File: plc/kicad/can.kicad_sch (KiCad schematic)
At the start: 12 parts, among them CN11 DB2ERC-5.08-4P, J3 Conn_01x02_Pin, SW4 MSK12C02, U18 TCAN337DR

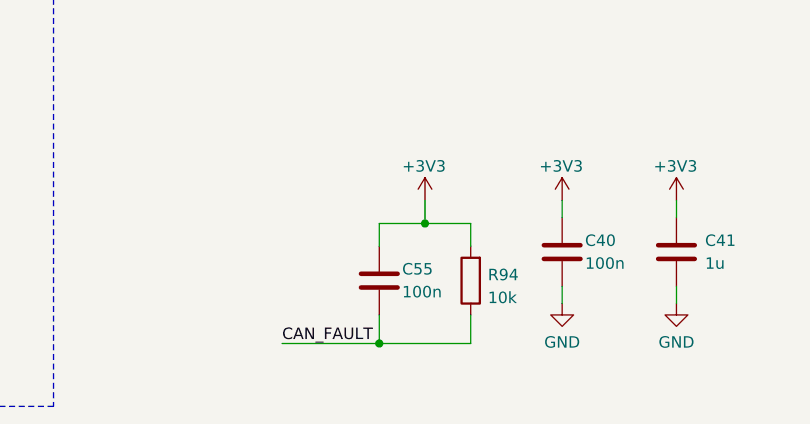
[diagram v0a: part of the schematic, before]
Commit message: Removed CAN FLT resistor
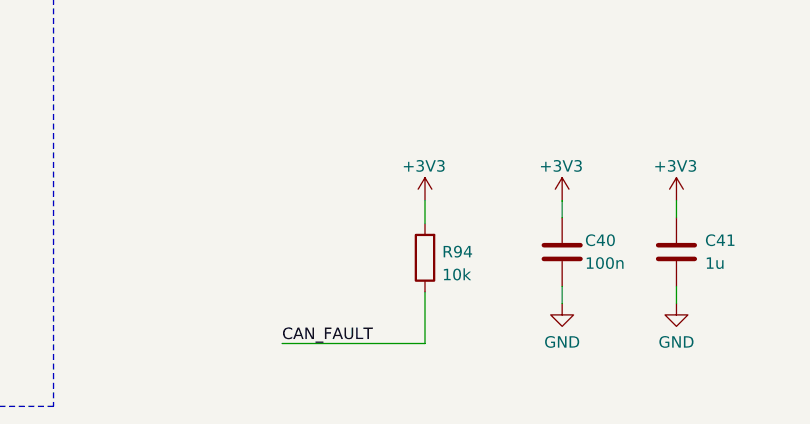
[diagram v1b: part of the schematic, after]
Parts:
- removed C55: 100n, Capacitor_SMD:C_0603_1608Metric, symbol Device:C
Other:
- moved on the sheet: R94
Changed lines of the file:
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@@
-	)
-	(junction
-		(at 160.02 159.385)
-		(diameter 0)
-		(color 0 0 0 0)
-	)
-	(junction
-		(at 165.1 146.05)
-		(diameter 0)
-		(color 0 0 0 0)
 	)
 	(junction
@@
 	(wire
 		(pts
-			(xy 170.18 146.05) (xy 170.18 148.59)
-		)
-		(stroke
-			(width 0)
-			(type default)
-		)
-	)
-	(wire
-		(pts
 			(xy 191.135 89.535) (xy 198.755 89.535)
 		)
@@
 	(wire
 		(pts
-			(xy 160.02 146.05) (xy 165.1 146.05)
-		)
-		(stroke
-			(width 0)
-			(type default)
-		)
-	)
-	(wire
-		(pts
 			(xy 57.15 81.915) (xy 74.295 81.915)
 		)
@@
 	(wire
 		(pts
-			(xy 160.02 156.21) (xy 160.02 159.385)
-		)
-		(stroke
-			(width 0)
-			(type default)
-		)
-	)
-	(wire
-		(pts
-			(xy 165.1 146.05) (xy 170.18 146.05)
-		)
-		(stroke
-			(width 0)
-			(type default)
-		)
-	)
-	(wire
-		(pts
 			(xy 69.215 106.045) (xy 69.215 104.775)
 		)
@@
 	(wire
 		(pts
-			(xy 160.02 159.385) (xy 170.18 159.385)
+			(xy 149.225 159.385) (xy 165.1 159.385)
 		)
 		(stroke
@@
 	(wire
 		(pts
-			(xy 149.225 159.385) (xy 160.02 159.385)
-		)
-		(stroke
-			(width 0)
-			(type default)
-		)
-	)
-	(wire
-		(pts
 			(xy 193.04 145.415) (xy 193.04 143.51)
 		)
@@
 	(wire
 		(pts
-			(xy 160.02 148.59) (xy 160.02 146.05)
-		)
-		(stroke
-			(width 0)
-			(type default)
-		)
-	)
-	(wire
-		(pts
 			(xy 76.835 147.955) (xy 79.375 147.955)
 		)
@@
 	(wire
 		(pts
-			(xy 170.18 159.385) (xy 170.18 156.21)
+			(xy 165.1 159.385) (xy 165.1 153.67)
 		)
 		(stroke
@@
 	)
 	(symbol
-		(lib_id "Device:C")
-		(at 160.02 152.4 0)
-		(unit 1)
-		(body_style 1)
-		(exclude_from_sim no)
-		(in_bom yes)
-		(on_board yes)
-		(in_pos_files yes)
-		(dnp no)
-		(property "Reference" "C55"
-			(at 162.56 151.13 0)
-			(show_name no)
-			(do_not_autoplace no)
-			(effects
-				(font
-					(size 1.27 1.27)
-				)
-				(justify left)
-			)
-		)
-		(property "Value" "100n"
-			(at 162.56 153.67 0)
-			(show_name no)
-			(do_not_autoplace no)
-			(effects
-				(font
-					(size 1.27 1.27)
-				)
-				(justify left)
-			)
-		)
-		(property "Footprint" "Capacitor_SMD:C_0603_1608Metric"
-			(at 160.9852 156.21 0)
-			(hide yes)
-			(show_name no)
-			(do_not_autoplace no)
-			(effects
-				(font
-					(size 1.27 1.27)
-				)
-			)
-		)
-		(property "Datasheet" ""
-			(at 160.02 152.4 0)
-			(hide yes)
-			(show_name no)
-			(do_not_autoplace no)
-			(effects
-				(font
-					(size 1.27 1.27)
-				)
-			)
-		)
-		(property "Description" "Unpolarized capacitor"
-			(at 160.02 152.4 0)
-			(hide yes)
-			(show_name no)
-			(do_not_autoplace no)
-			(effects
-				(font
-					(size 1.27 1.27)
-				)
-			)
-		)
-		(pin "2"
-		)
-		(pin "1"
-		)
-		(instances
-			(project "LibrePLC32"
-				(path "/ef4c1a27-85a3-413a-9f93-a41c4f97eee5/1f15b1b2-5031-4e14-8391-148d71dbf666"
-					(reference "C55")
-					(unit 1)
-				)
-			)
-		)
-	)
-	(symbol
 		(lib_id "LibrePLC32:SM24CANA-02HTG")
 		(at 69.215 97.155 180)
@@
 	(symbol
 		(lib_id "Device:R")
-		(at 170.18 152.4 180)
+		(at 165.1 149.86 180)
 		(unit 1)
 		(body_style 1)
@@
 		(dnp no)
 		(property "Reference" "R94"
-			(at 172.085 151.765 0)
+			(at 167.005 149.225 0)
 			(show_name no)
 			(do_not_autoplace no)
@@
 		)
 		(property "Value" "10k"
-			(at 172.085 154.305 0)
+			(at 167.005 151.765 0)
 			(show_name no)
 			(do_not_autoplace no)
@@
 		)
 		(property "Footprint" "Resistor_SMD:R_0603_1608Metric"
-			(at 171.958 152.4 90)
+			(at 166.878 149.86 90)
 			(hide yes)
 			(show_name no)
@@
 		)
 		(property "Datasheet" ""
-			(at 170.18 152.4 0)
+			(at 165.1 149.86 0)
 			(hide yes)
 			(show_name no)
@@
 		)
 		(property "Description" "Resistor"
-			(at 170.18 152.4 0)
-			(hide yes)
-			(show_name no)
+			(at 165.1 149.86 0)
+			(hide yes)
+			(show_name no)

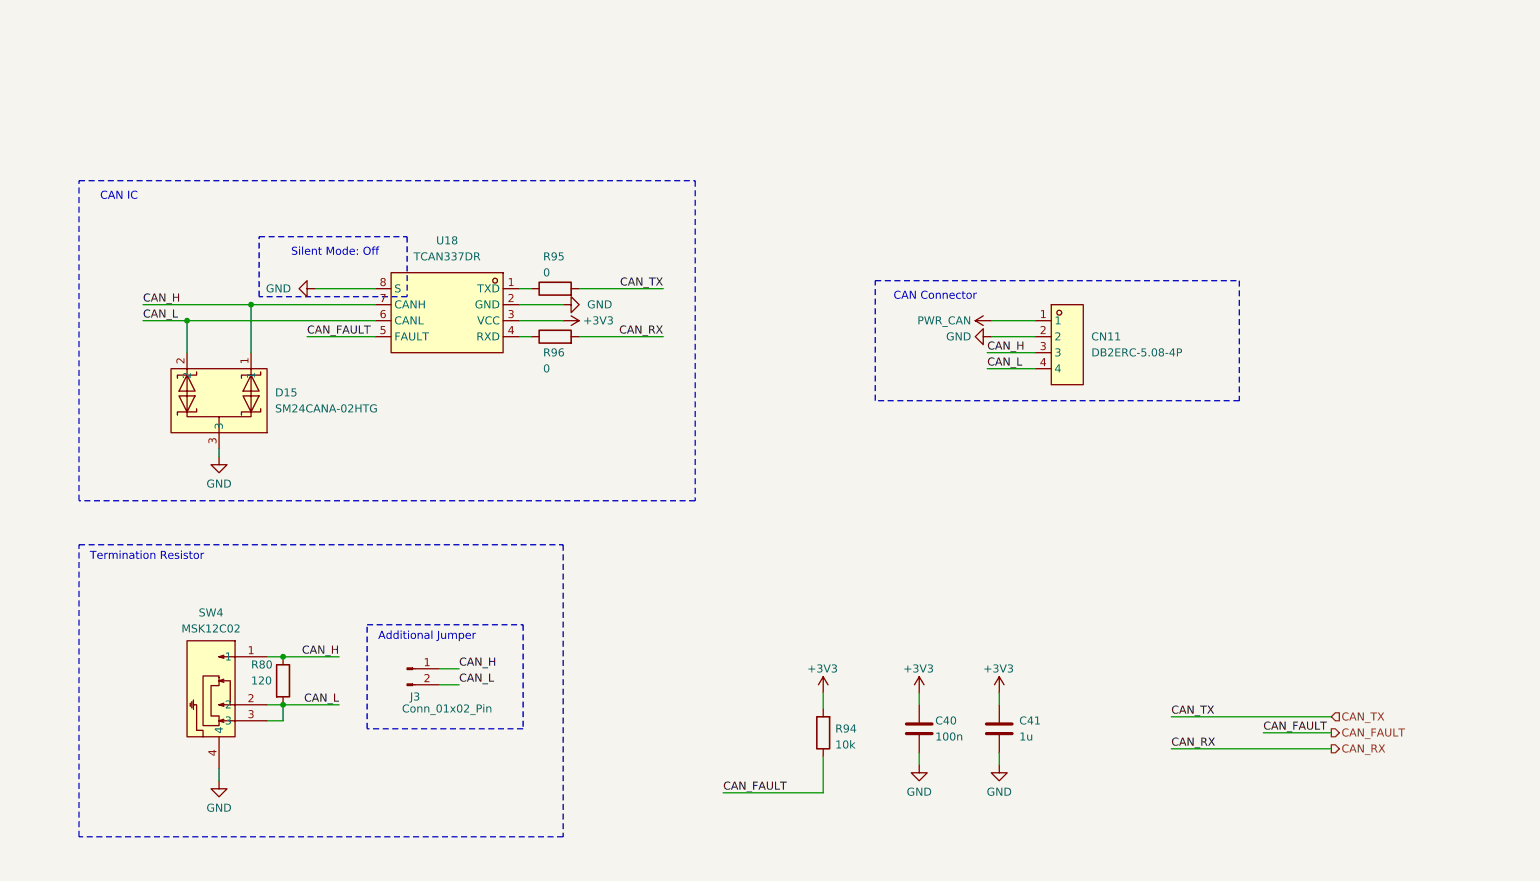
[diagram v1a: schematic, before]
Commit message: Rearranged small PCB placements
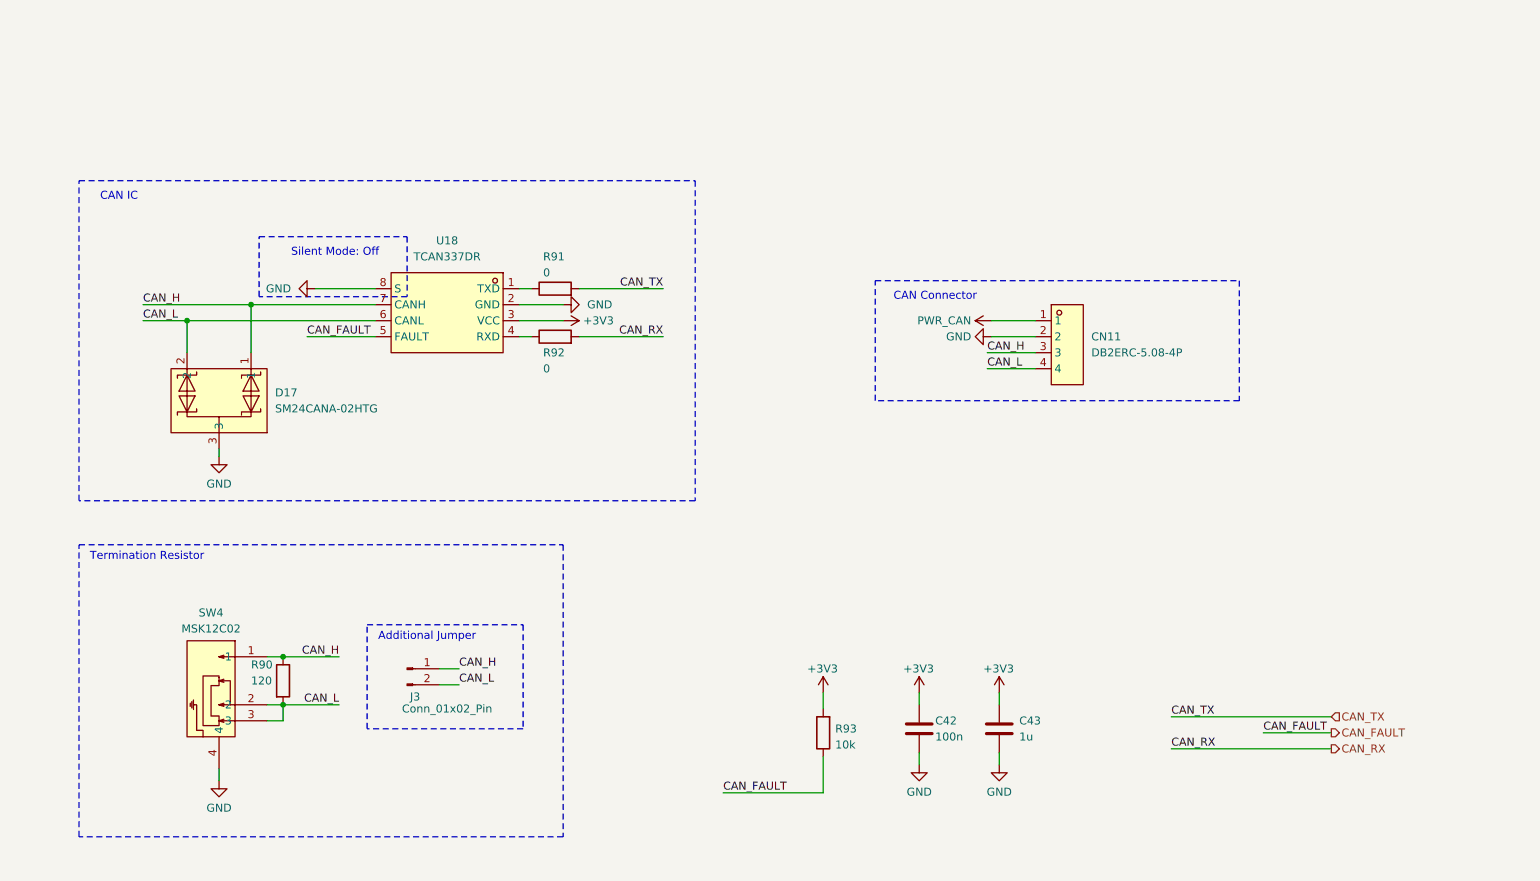
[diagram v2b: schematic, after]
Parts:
- renumbered C40 to C42, C41 to C43, D15 to D17, R80 to R90, R95 to R91, R96 to R92, R94 to R93
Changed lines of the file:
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@@
 		(in_pos_files yes)
 		(dnp no)
-		(property "Reference" "#PWR0199"
+		(property "Reference" "#PWR0212"
 			(at 193.04 147.32 0)
 			(hide yes)
@@
 			(project "LibrePLC32"
 				(path "/ef4c1a27-85a3-413a-9f93-a41c4f97eee5/1f15b1b2-5031-4e14-8391-148d71dbf666"
-					(reference "#PWR0199")
+					(reference "#PWR0212")
 					(unit 1)
 				)
@@
 		(dnp no)
 		(fields_autoplaced yes)
-		(property "Reference" "#PWR0200"
+		(property "Reference" "#PWR0213"
 			(at 193.04 161.29 0)
 			(hide yes)
@@
 			(project "LibrePLC32"
 				(path "/ef4c1a27-85a3-413a-9f93-a41c4f97eee5/1f15b1b2-5031-4e14-8391-148d71dbf666"
-					(reference "#PWR0200")
+					(reference "#PWR0213")
 					(unit 1)
 				)
@@
 		(in_pos_files yes)
 		(dnp no)
-		(property "Reference" "#PWR0192"
+		(property "Reference" "#PWR0204"
 			(at 78.105 79.375 0)
 			(hide yes)
@@
 			(project "LibrePLC32"
 				(path "/ef4c1a27-85a3-413a-9f93-a41c4f97eee5/1f15b1b2-5031-4e14-8391-148d71dbf666"
-					(reference "#PWR0192")
+					(reference "#PWR0204")
 					(unit 1)
 				)
@@
 		(in_pos_files yes)
 		(dnp no)
-		(property "Reference" "#PWR0247"
+		(property "Reference" "#PWR0207"
 			(at 165.1 147.32 0)
 			(hide yes)
@@
 			(project "LibrePLC32"
 				(path "/ef4c1a27-85a3-413a-9f93-a41c4f97eee5/1f15b1b2-5031-4e14-8391-148d71dbf666"
-					(reference "#PWR0247")
+					(reference "#PWR0207")
 					(unit 1)
 				)
@@
 		(dnp no)
 		(fields_autoplaced yes)
-		(property "Reference" "#PWR0190"
+		(property "Reference" "#PWR0203"
 			(at 69.215 163.83 0)
 			(hide yes)
@@
 			(project "LibrePLC32"
 				(path "/ef4c1a27-85a3-413a-9f93-a41c4f97eee5/1f15b1b2-5031-4e14-8391-148d71dbf666"
-					(reference "#PWR0190")
+					(reference "#PWR0203")
 					(unit 1)
 				)
@@
 		(dnp no)
 		(fields_autoplaced yes)
-		(property "Reference" "D15"
+		(property "Reference" "D17"
 			(at 78.105 95.8849 0)
 			(show_name no)
@@
 			(project "LibrePLC32"
 				(path "/ef4c1a27-85a3-413a-9f93-a41c4f97eee5/1f15b1b2-5031-4e14-8391-148d71dbf666"
-					(reference "D15")
+					(reference "D17")
 					(unit 1)
 				)
@@
 		(in_pos_files yes)
 		(dnp no)
-		(property "Reference" "#PWR0194"
+		(property "Reference" "#PWR0206"
 			(at 120.015 84.455 0)
 			(hide yes)
@@
 			(project "LibrePLC32"
 				(path "/ef4c1a27-85a3-413a-9f93-a41c4f97eee5/1f15b1b2-5031-4e14-8391-148d71dbf666"
-					(reference "#PWR0194")
+					(reference "#PWR0206")
 					(unit 1)
 				)
@@
 		(in_pos_files yes)
 		(dnp no)
-		(property "Reference" "C40"
+		(property "Reference" "C42"
 			(at 182.88 147.955 0)
 			(show_name no)
@@
 			(project "LibrePLC32"
 				(path "/ef4c1a27-85a3-413a-9f93-a41c4f97eee5/1f15b1b2-5031-4e14-8391-148d71dbf666"
-					(reference "C40")
+					(reference "C42")
 					(unit 1)
 				)
@@
 		(in_pos_files yes)
 		(dnp no)
-		(property "Reference" "R95"
+		(property "Reference" "R91"
 			(at 120.65 74.295 90)
 			(show_name no)
@@
 			(project "LibrePLC32"
 				(path "/ef4c1a27-85a3-413a-9f93-a41c4f97eee5/1f15b1b2-5031-4e14-8391-148d71dbf666"
-					(reference "R95")
+					(reference "R91")
 					(unit 1)
 				)
@@
 		(in_pos_files yes)
 		(dnp no)
-		(property "Reference" "#PWR0193"
+		(property "Reference" "#PWR0205"
 			(at 130.175 81.915 0)
 			(hide yes)
@@
 			(project "LibrePLC32"
 				(path "/ef4c1a27-85a3-413a-9f93-a41c4f97eee5/1f15b1b2-5031-4e14-8391-148d71dbf666"
-					(reference "#PWR0193")
+					(reference "#PWR0205")
 					(unit 1)
 				)
@@
 		(in_pos_files yes)
 		(dnp no)
-		(property "Reference" "R80"
+		(property "Reference" "R90"
 			(at 74.295 139.065 0)
 			(show_name no)
@@
 			(project "LibrePLC32"
 				(path "/ef4c1a27-85a3-413a-9f93-a41c4f97eee5/1f15b1b2-5031-4e14-8391-148d71dbf666"
-					(reference "R80")
+					(reference "R90")
 					(unit 1)
 				)
@@
 		(in_pos_files yes)
 		(dnp no)
-		(property "Reference" "R96"
+		(property "Reference" "R92"
 			(at 120.65 89.535 90)
 			(show_name no)
@@
 			(project "LibrePLC32"
 				(path "/ef4c1a27-85a3-413a-9f93-a41c4f97eee5/1f15b1b2-5031-4e14-8391-148d71dbf666"
-					(reference "R96")
+					(reference "R92")
 					(unit 1)
 				)
@@
 		(in_pos_files yes)
 		(dnp no)
-		(property "Reference" "R94"
+		(property "Reference" "R93"
 			(at 167.005 149.225 0)
 			(show_name no)
@@
 			(project "LibrePLC32"
 				(path "/ef4c1a27-85a3-413a-9f93-a41c4f97eee5/1f15b1b2-5031-4e14-8391-148d71dbf666"
-					(reference "R94")
+					(reference "R93")
 					(unit 1)
 				)
@@
 		(in_pos_files yes)
 		(dnp no)
-		(property "Reference" "C41"
+		(property "Reference" "C43"
 			(at 196.215 147.955 0)
 			(show_name no)
@@
 			(project "LibrePLC32"
 				(path "/ef4c1a27-85a3-413a-9f93-a41c4f97eee5/1f15b1b2-5031-4e14-8391-148d71dbf666"
-					(reference "C41")
+					(reference "C43")
 					(unit 1)
 				)
@@
 		(dnp no)
 		(fields_autoplaced yes)
-		(property "Reference" "#PWR0198"
+		(property "Reference" "#PWR0211"
 			(at 185.42 86.995 0)
 			(hide yes)
@@
 			(project "LibrePLC32"
 				(path "/ef4c1a27-85a3-413a-9f93-a41c4f97eee5/1f15b1b2-5031-4e14-8391-148d71dbf666"
-					(reference "#PWR0198")
+					(reference "#PWR0211")
 					(unit 1)
 				)
@@
 		(dnp no)
 		(fields_autoplaced yes)
-		(property "Reference" "#PWR0196"
+		(property "Reference" "#PWR0209"
 			(at 180.34 161.29 0)
 			(hide yes)
@@
 			(project "LibrePLC32"
 				(path "/ef4c1a27-85a3-413a-9f93-a41c4f97eee5/1f15b1b2-5031-4e14-8391-148d71dbf666"
-					(reference "#PWR0196")
+					(reference "#PWR0209")
 					(unit 1)
 				)
@@
 		(dnp no)
 		(fields_autoplaced yes)
-		(property "Reference" "#PWR0197"
+		(property "Reference" "#PWR0210"
 			(at 195.58 84.455 0)
 			(hide yes)
@@
 			(project "LibrePLC32"
 				(path "/ef4c1a27-85a3-413a-9f93-a41c4f97eee5/1f15b1b2-5031-4e14-8391-148d71dbf666"
-					(reference "#PWR0197")
+					(reference "#PWR0210")
 					(unit 1)
 				)
@@
 		(dnp no)
 		(fields_autoplaced yes)
-		(property "Reference" "#PWR0191"
+		(property "Reference" "#PWR0202"
 			(at 69.215 112.395 0)
 			(hide yes)
@@
 			(project "LibrePLC32"
 				(path "/ef4c1a27-85a3-413a-9f93-a41c4f97eee5/1f15b1b2-5031-4e14-8391-148d71dbf666"
-					(reference "#PWR0191")
+					(reference "#PWR0202")
 					(unit 1)
 				)
@@
 		(in_pos_files yes)
 		(dnp no)
-		(property "Reference" "#PWR0195"
+		(property "Reference" "#PWR0208"
 			(at 180.34 147.32 0)
 			(hide yes)
@@
 			(project "LibrePLC32"
 				(path "/ef4c1a27-85a3-413a-9f93-a41c4f97eee5/1f15b1b2-5031-4e14-8391-148d71dbf666"
-					(reference "#PWR0195")
-					(unit 1)
-				)
+					(reference "#PWR0208")
+					(unit 1)
+				)

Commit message: Updated PCB placement
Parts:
- J3: footprint Connector_PinSocket_2.54mm:PinSocket_1x02_P2.54mm_Vertical -> Connector_PinHeader_2.54mm:PinHeader_1x02_P2.54mm_Vertical
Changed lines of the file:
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@@
 			)
 		)
-		(property "Footprint" "Connector_PinSocket_2.54mm:PinSocket_1x02_P2.54mm_Vertical"
+		(property "Footprint" "Connector_PinHeader_2.54mm:PinHeader_1x02_P2.54mm_Vertical"
 			(at 99.06 139.7 0)
 			(hide yes)
